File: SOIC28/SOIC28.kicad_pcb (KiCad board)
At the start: 2 copper layers, 35.6 x 17.8 mm, 7 parts, among them J1 Conn_01x14, J2 Conn_02x14_Counter_Clockwise, J3 Conn_01x14, J4 Conn_02x14_Counter_Clockwise

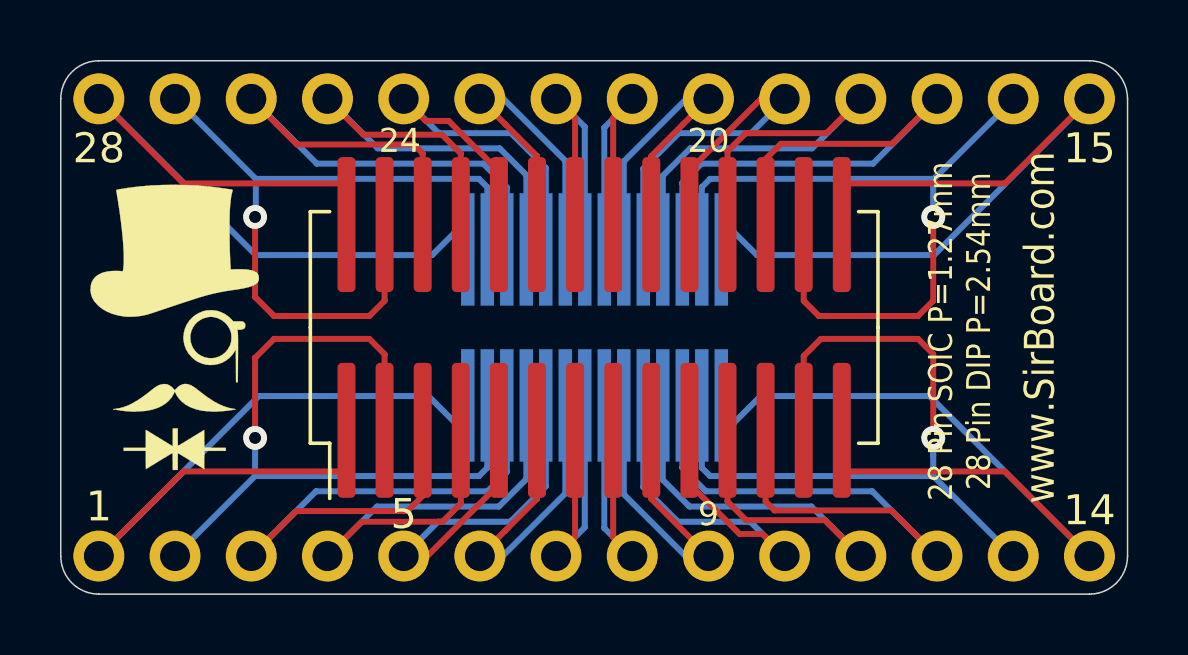
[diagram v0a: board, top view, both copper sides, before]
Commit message: Breakout Boards Revision 2
Renders updated, silkscreen text improved, blurry silkscreen items removed/resized.
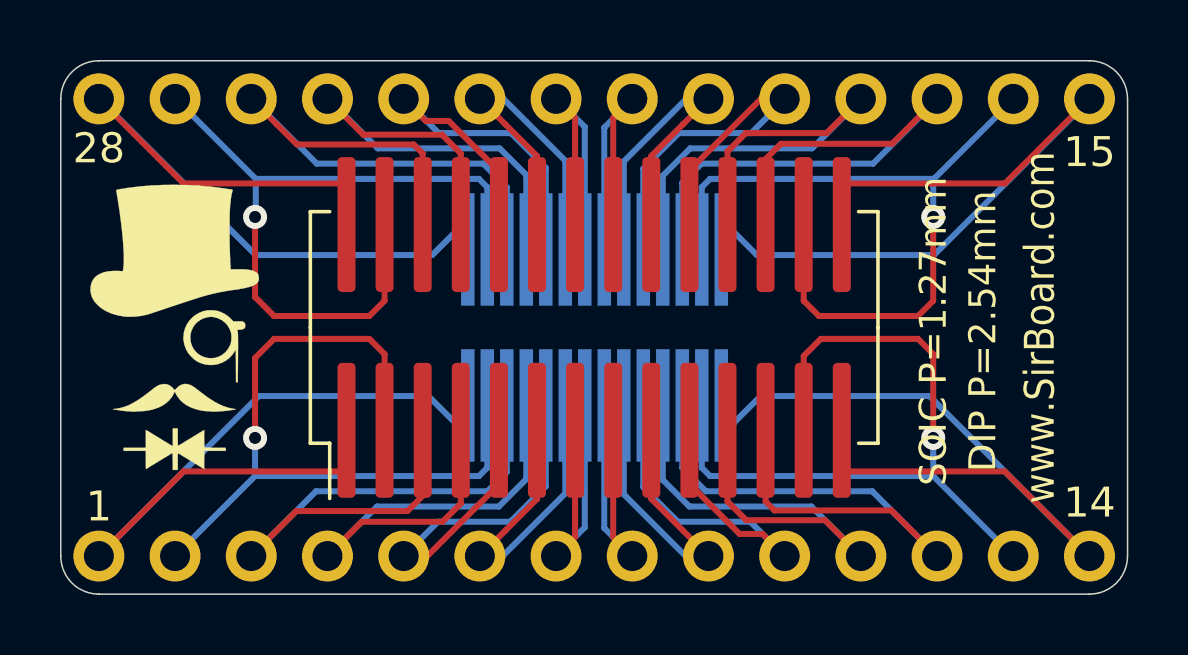
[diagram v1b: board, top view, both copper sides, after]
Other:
- board text added: "DIP P=2.54mm"
- board text added: "SOIC P=1.27mm"
- board text added: "TSSOP P=0.65mm"
- board text removed: "28 Pin DIP P=2.54mm"
- board text removed: "28 Pin SOIC P=1.27mm"
- board text removed: "28 Pin TSSOP P=0.65mm"
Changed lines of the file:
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@@
   (general
     (thickness 1.6)
-    (drawings 34)
+    (drawings 30)
     (tracks 207)
     (zones 0)
@@
   (title_block
     (title "SOIC28 To DIP28 Breakout Board")
-    (date 2019-07-10)
-    (rev 1)
+    (date 2020-04-18)
+    (rev 2)
     (company SirBoard)
     (comment 1 "SOIC P = 1.27mm")
@@
     (solder_mask_min_width 0.1)
     (aux_axis_origin 0 0)
+    (grid_origin 48.895 29.718)
     (visible_elements 7FFFFFFF)
     (pcbplotparams
@@
     (effects (font (size 1 1) (thickness 0.15)))
   )
-  (gr_text 14 (at 50.165 44.704) (layer B.SilkS)
-    (effects (font (size 1 1) (thickness 0.15)) (justify mirror))
-  )
-  (gr_text 28 (at 83.185 32.639) (layer B.SilkS)
-    (effects (font (size 1 1) (thickness 0.15)) (justify mirror))
-  )
-  (gr_text 9 (at 62.865 44.577) (layer B.SilkS)
+  (gr_text 14 (at 50.165 44.45) (layer B.SilkS)
     (effects (font (size 1 1) (thickness 0.12)) (justify mirror))
   )
-  (gr_text 15 (at 50.038 32.639) (layer B.SilkS)
-    (effects (font (size 1 1) (thickness 0.15)) (justify mirror))
-  )
-  (gr_text 20 (at 62.865 32.639) (layer B.SilkS)
-    (effects (font (size 1 1) (thickness 0.15)) (justify mirror))
-  )
-  (gr_text 5 (at 73.025 44.704) (layer B.SilkS)
-    (effects (font (size 1 1) (thickness 0.15)) (justify mirror))
-  )
-  (gr_text 1 (at 83.185 44.704) (layer B.SilkS)
-    (effects (font (size 1 1) (thickness 0.15)) (justify mirror))
-  )
-  (gr_text 24 (at 73.025 32.639) (layer B.SilkS)
-    (effects (font (size 1 1) (thickness 0.15)) (justify mirror))
+  (gr_text 28 (at 83.185 32.766) (layer B.SilkS)
+    (effects (font (size 1 1) (thickness 0.12)) (justify mirror))
+  )
+  (gr_text 9 (at 62.865 44.45) (layer B.SilkS)
+    (effects (font (size 1 1) (thickness 0.12)) (justify mirror))
+  )
+  (gr_text 15 (at 50.165 32.766) (layer B.SilkS)
+    (effects (font (size 1 1) (thickness 0.12)) (justify mirror))
+  )
+  (gr_text 20 (at 62.865 32.766) (layer B.SilkS)
+    (effects (font (size 1 1) (thickness 0.12)) (justify mirror))
+  )
+  (gr_text 5 (at 73.025 44.45) (layer B.SilkS)
+    (effects (font (size 1 1) (thickness 0.12)) (justify mirror))
+  )
+  (gr_text 1 (at 83.185 44.45) (layer B.SilkS)
+    (effects (font (size 1 1) (thickness 0.12)) (justify mirror))
+  )
+  (gr_text 24 (at 73.025 32.766) (layer B.SilkS)
+    (effects (font (size 1 1) (thickness 0.12)) (justify mirror))
   )
   (gr_text 28 (at 50.165 32.639) (layer F.SilkS)
     (effects (font (size 1 1) (thickness 0.15)))
   )
-  (gr_text 24 (at 60.198 32.385) (layer F.SilkS)
-    (effects (font (size 0.8 0.8) (thickness 0.13)))
-  )
-  (gr_text 20 (at 70.485 32.385) (layer F.SilkS)
-    (effects (font (size 0.8 0.8) (thickness 0.13)))
-  )
-  (gr_text 15 (at 83.185 32.639) (layer F.SilkS)
-    (effects (font (size 1 1) (thickness 0.15)))
-  )
-  (gr_text 14 (at 83.185 44.704) (layer F.SilkS)
-    (effects (font (size 1 1) (thickness 0.15)))
-  )
-  (gr_text 9 (at 70.485 44.831) (layer F.SilkS)
-    (effects (font (size 0.8 0.8) (thickness 0.13)))
-  )
-  (gr_text 5 (at 60.325 44.831) (layer F.SilkS)
-    (effects (font (size 1 1) (thickness 0.15)))
-  )
-  (gr_text "28 Pin DIP P=2.54mm\n" (at 54.229 38.608 270) (layer B.SilkS)
-    (effects (font (size 0.8 0.7) (thickness 0.15)) (justify mirror))
-  )
-  (gr_text "28 Pin TSSOP P=0.65mm" (at 55.626 38.608 270) (layer B.SilkS)
-    (effects (font (size 0.8 0.7) (thickness 0.15)) (justify mirror))
+  (gr_text 15 (at 83.185 32.766) (layer F.SilkS)
+    (effects (font (size 1 1) (thickness 0.12)))
+  )
+  (gr_text 14 (at 83.185 44.45) (layer F.SilkS)
+    (effects (font (size 1 1) (thickness 0.12)))
+  )
+  (gr_text "DIP P=2.54mm\n" (at 54.229 38.608 270) (layer B.SilkS)
+    (effects (font (size 0.9 0.9) (thickness 0.12)) (justify mirror))
+  )
+  (gr_text "TSSOP P=0.65mm" (at 55.626 38.608 270) (layer B.SilkS)
+    (effects (font (size 0.9 0.9) (thickness 0.12)) (justify mirror))
   )
   (gr_text www.SirBoard.com (at 52.07 38.608 270) (layer B.SilkS)
-    (effects (font (size 1 0.9) (thickness 0.15)) (justify mirror))
-  )
-  (gr_text "28 Pin DIP P=2.54mm" (at 79.502 38.735 90) (layer F.SilkS)
-    (effects (font (size 0.8 0.7) (thickness 0.15)))
-  )
-  (gr_text "28 Pin SOIC P=1.27mm" (at 78.232 38.735 90) (layer F.SilkS)
-    (effects (font (size 0.8 0.7) (thickness 0.15)))
+    (effects (font (size 1 0.9) (thickness 0.13)) (justify mirror))
+  )
+  (gr_text "DIP P=2.54mm" (at 79.629 38.735 90) (layer F.SilkS)
+    (effects (font (size 0.9 0.9) (thickness 0.12)))
+  )
+  (gr_text "SOIC P=1.27mm" (at 77.978 38.735 90) (layer F.SilkS)
+    (effects (font (size 0.9 0.9) (thickness 0.12)))
   )
   (gr_text www.SirBoard.com (at 81.534 38.608 90) (layer F.SilkS)
-    (effects (font (size 1 0.9) (thickness 0.15)))
+    (effects (font (size 1 0.9) (thickness 0.13)))
   )
   (segment (start 80.365 43.408) (end 83.185 46.228) (width 0.2) (layer F.Cu) (net 1))
